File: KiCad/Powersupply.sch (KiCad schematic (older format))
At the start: 9 parts, among them J501 12V, U501 LM1086-5V, U502 LM1086-3.3V

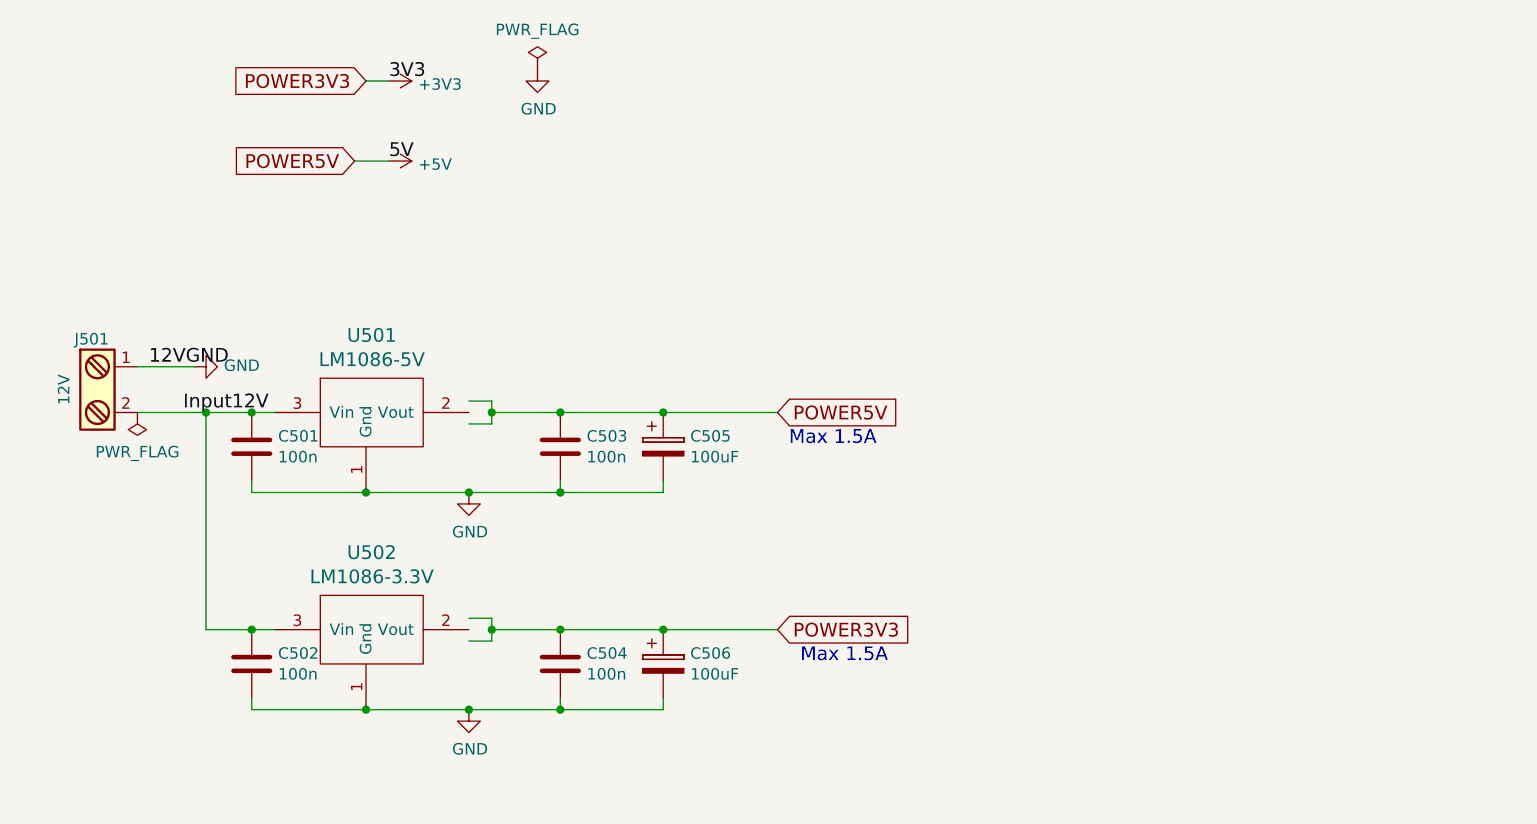
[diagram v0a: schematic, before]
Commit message: Before reworking analog inputs.
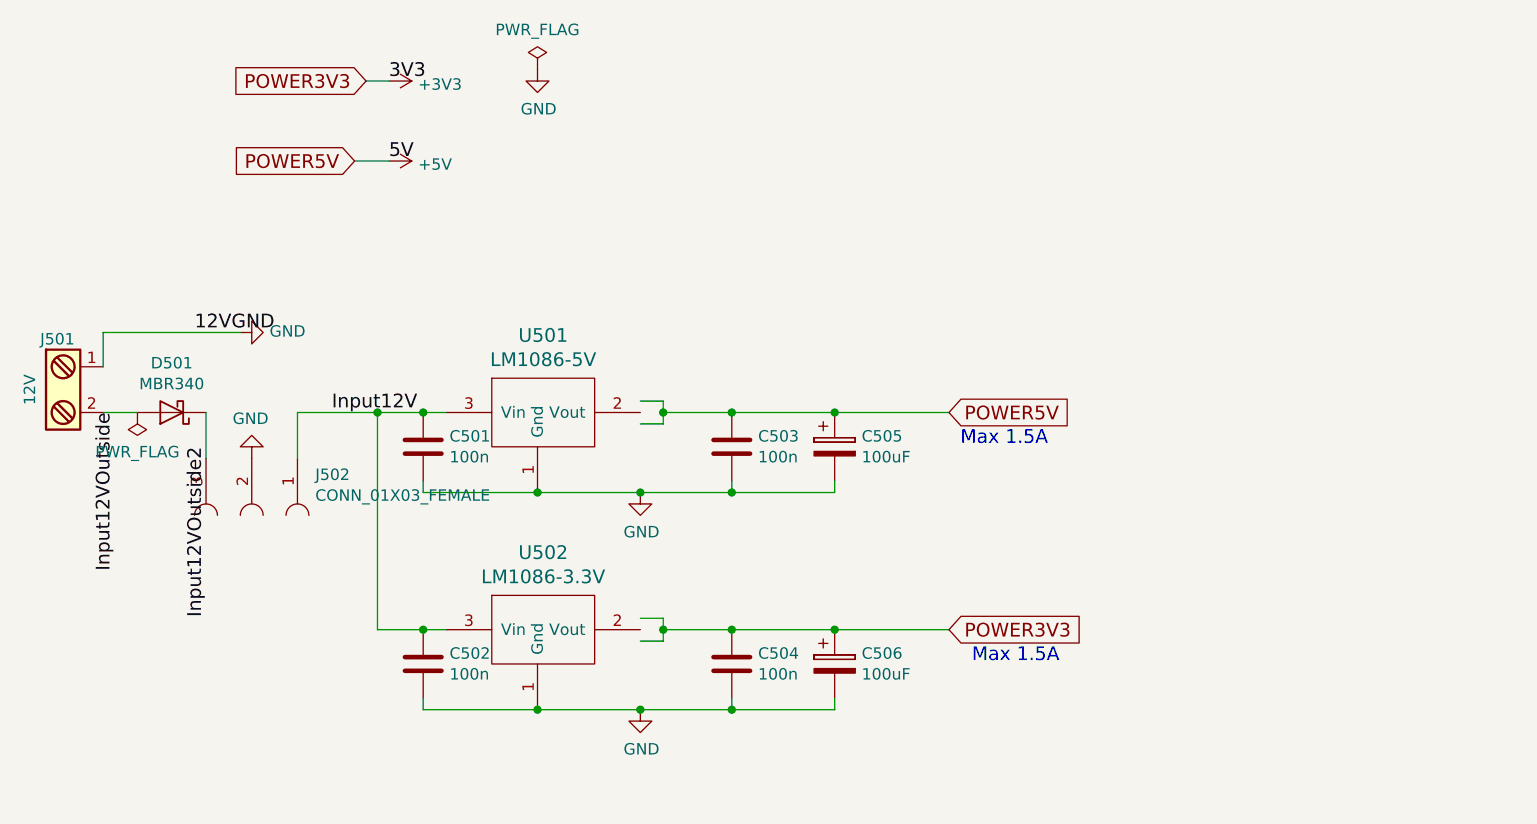
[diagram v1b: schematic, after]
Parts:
- added D501: MBR340, Diodes_SMD:D_SMB, symbol MBR340
- added J502: CONN_01X03_FEMALE, Pin_Headers:Pin_Header_Straight_1x03_Pitch2.54mm, symbol CONN_01X03_FEMALE
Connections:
- net labels added: Input12VOutside, Input12VOutside2
- wire segments 22 -> 26
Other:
- moved on the sheet: C501, C502, C503, C504, C505, C506, J501, U501, U502

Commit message: Save with sensor inputs using digital potentiometer
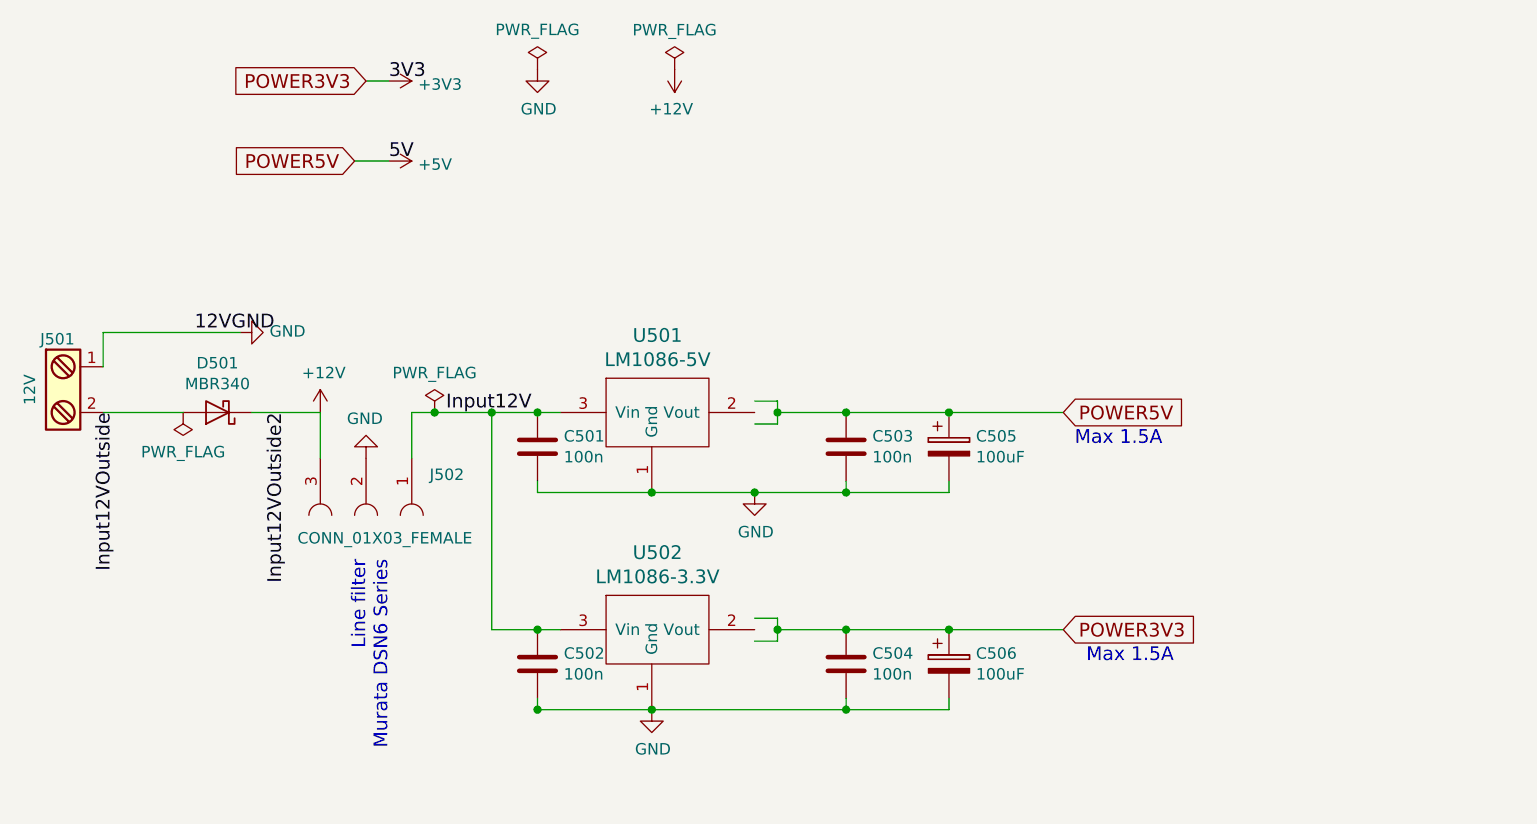
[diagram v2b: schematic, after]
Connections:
- net labels added: +12V
- wire segments 26 -> 27
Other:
- note added: "Line filter\nMurata DSN6 Series"
- moved on the sheet: C501, C502, C503, C504, C505, C506, D501, J502, U501, U502

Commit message: Inputs reworked. New terminals
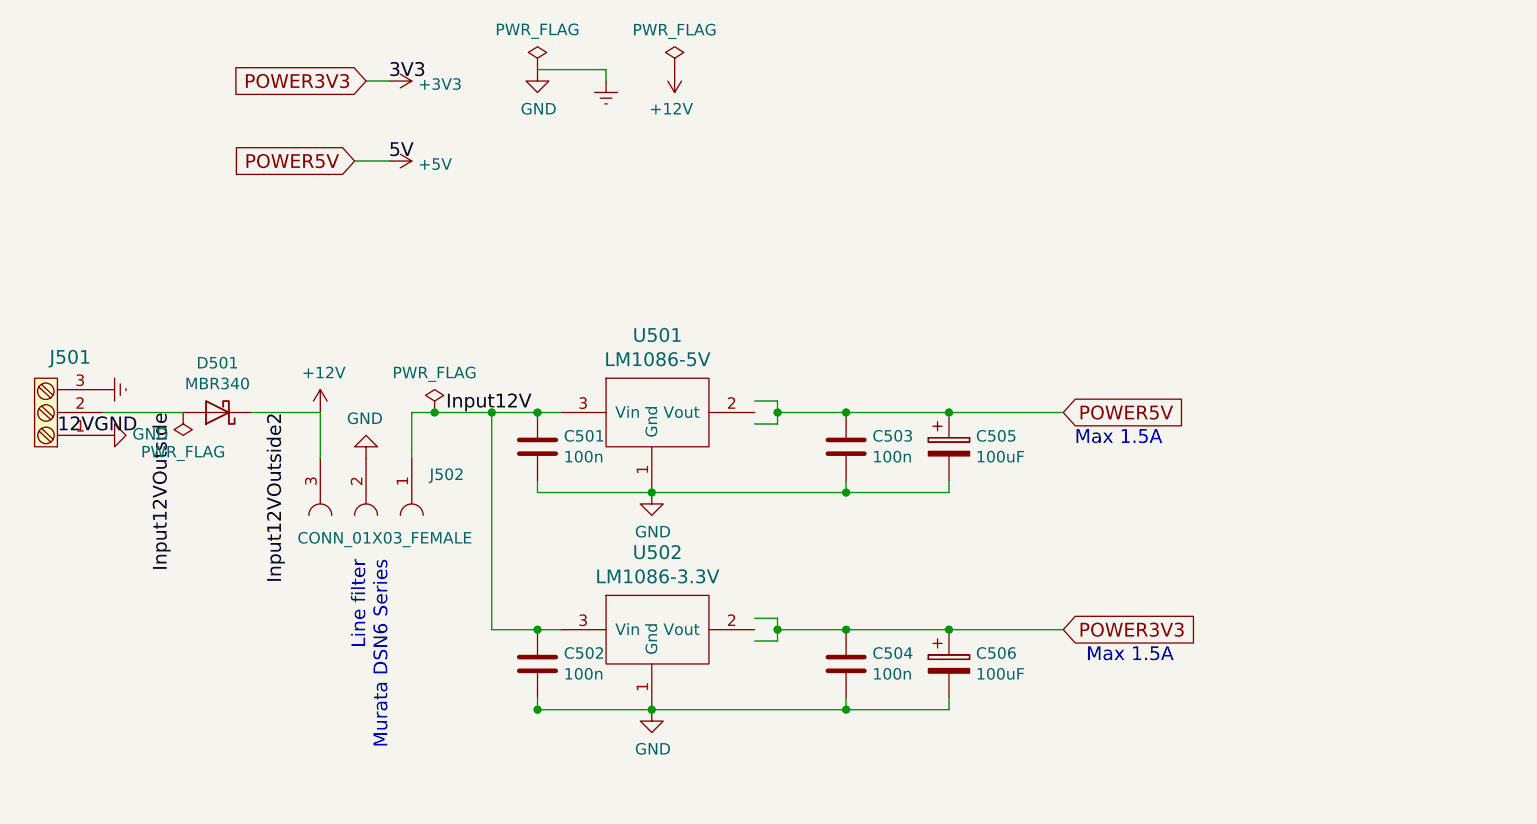
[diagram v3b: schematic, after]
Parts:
- removed J501: 12V, Connectors_Terminal_Blocks:TerminalBlock_Pheonix_MPT-2.54mm_2pol, symbol Screw_Terminal_1x02
- added J501: TE_Connectivity_282834-3, TE_Connectivity:TE_Connectivity_282834-3, symbol TE_Connectivity_282834-3
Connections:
- net labels added: Earth
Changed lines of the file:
@@
 LIBS:LM1086
 LIBS:X95840WV20IZ-2_7T1
-LIBS:804-112
+LIBS:TE_Connectivity
 LIBS:HAP-IO-Card-cache
 EELAYER 26 0
@@
 POWER3V3
 $Comp
-L +3V3 #PWR0118
+L +3V3 #PWR0104
 U 1 1 592AD7CB
 P 2200 1500
-F 0 "#PWR0118" H 2200 1350 50  0001 C CNN
+F 0 "#PWR0104" H 2200 1350 50  0001 C CNN
 F 1 "+3V3" V 2215 1628 50  0000 L CNN
 F 2 "" H 2200 1500 50  0001 C CNN
@@
 	2100 1500 2200 1500
 $Comp
-L PWR_FLAG #FLG0119
+L PWR_FLAG #FLG0105
 U 1 1 592B4E13
 P 2850 1450
-F 0 "#FLG0119" H 2850 1525 50  0001 C CNN
+F 0 "#FLG0105" H 2850 1525 50  0001 C CNN
 F 1 "PWR_FLAG" H 2850 1624 50  0000 C CNN
 F 2 "" H 2850 1450 50  0001 C CNN
@@
 $EndComp
 $Comp
-L GND #PWR0120
+L GND #PWR0106
 U 1 1 592B4E96
 P 2850 1450
-F 0 "#PWR0120" H 2850 1200 50  0001 C CNN
+F 0 "#PWR0106" H 2850 1200 50  0001 C CNN
 F 1 "GND" H 2855 1277 50  0000 C CNN
 F 2 "" H 2850 1450 50  0001 C CNN
@@
 $EndComp
 $Comp
-L GND #PWR0121
+L GND #PWR0107
 U 1 1 5924C039
 P 3350 4250
-F 0 "#PWR0121" H 3350 4000 50  0001 C CNN
+F 0 "#PWR0107" H 3350 4000 50  0001 C CNN
 F 1 "GND" H 3355 4077 50  0000 C CNN
 F 2 "" H 3350 4250 50  0001 C CNN
@@
 Connection ~ 4200 2950
 $Comp
-L GND #PWR0122
+L GND #PWR0108
 U 1 1 5924DE85
-P 1550 2600
-F 0 "#PWR0122" H 1550 2350 50  0001 C CNN
-F 1 "GND" V 1555 2472 50  0000 R CNN
-F 2 "" H 1550 2600 50  0001 C CNN
-F 3 "" H 1550 2600 50  0001 C CNN
-	1    1550 2600
+P 950 3050
+F 0 "#PWR0108" H 950 2800 50  0001 C CNN
+F 1 "GND" V 955 2922 50  0000 R CNN
+F 2 "" H 950 3050 50  0001 C CNN
+F 3 "" H 950 3050 50  0001 C CNN
+	1    950  3050
 	0    -1   -1   0
 $EndComp
 $Comp
-L PWR_FLAG #FLG0123
+L PWR_FLAG #FLG0109
 U 1 1 5924DE8B
 P 1300 2950
-F 0 "#FLG0123" H 1300 3025 50  0001 C CNN
+F 0 "#FLG0109" H 1300 3025 50  0001 C CNN
 F 1 "PWR_FLAG" H 1300 3123 50  0000 C CNN
 F 2 "" H 1300 2950 50  0001 C CNN
@@
 $EndComp
 Connection ~ 2850 2950
-$Comp
-L Screw_Terminal_1x02 J501
-U 1 1 5924DE7F
-P 750 2850
-F 0 "J501" H 750 3100 50  0000 C TNN
-F 1 "12V" V 600 2850 50  0000 C TNN
-F 2 "Connectors_Terminal_Blocks:TerminalBlock_Pheonix_MPT-2.54mm_2pol" H 750 2625 50  0001 C CNN
-F 3 "" H 725 2850 50  0001 C CNN
-	1    750  2850
-	1    0    0    -1
-$EndComp
 Wire Wire Line
 	2650 2950 2650 3900
@@
 	2050 1850 2200 1850
 $Comp
-L +5V #PWR0124
+L +5V #PWR0110
 U 1 1 5924EF19
 P 2200 1850
-F 0 "#PWR0124" H 2200 1700 50  0001 C CNN
+F 0 "#PWR0110" H 2200 1700 50  0001 C CNN
 F 1 "+5V" V 2215 1978 50  0000 L CNN
 F 2 "" H 2200 1850 50  0001 C CNN
@@
 $EndComp
 $Comp
-L GND #PWR0125
+L GND #PWR0111
 U 1 1 5924DE5E
-P 3800 3300
-F 0 "#PWR0125" H 3800 3050 50  0001 C CNN
-F 1 "GND" H 3805 3127 50  0000 C CNN
-F 2 "" H 3800 3300 50  0001 C CNN
-F 3 "" H 3800 3300 50  0001 C CNN
-	1    3800 3300
+P 3350 3300
+F 0 "#PWR0111" H 3350 3050 50  0001 C CNN
+F 1 "GND" H 3355 3127 50  0000 C CNN
+F 2 "" H 3350 3300 50  0001 C CNN
+F 3 "" H 3350 3300 50  0001 C CNN
+	1    3350 3300
 	1    0    0    -1
 $EndComp
@@
 Wire Wire Line
 	4200 3300 4200 3250
-Connection ~ 3800 3300
 Connection ~ 4200 3300
 Wire Wire Line
@@
 	1    0    0    -1
 $EndComp
-Wire Wire Line
-	950  2600 1550 2600
-Text Label 1350 2600 0    60   ~ 0
+Text Label 750  3050 0    60   ~ 0
 12VGND
 $Comp
@@
 	-1   0    0    1
 $EndComp
-Text Label 1000 2950 3    60   ~ 0
+Text Label 1250 2950 3    60   ~ 0
 Input12VOutside
 Wire Wire Line
@@
 $EndComp
 $Comp
-L GND #PWR0126
+L GND #PWR0112
 U 1 1 592909E6
 P 2100 3150
-F 0 "#PWR0126" H 2100 2900 50  0001 C CNN
+F 0 "#PWR0112" H 2100 2900 50  0001 C CNN
 F 1 "GND" H 2105 2977 50  0000 C CNN
 F 2 "" H 2100 3150 50  0001 C CNN
@@
 	-1   0    0    1
 $EndComp
-Wire Wire Line
-	950  2600 950  2750
 Text Label 1750 2950 3    60   ~ 0
 Input12VOutside2
@@
 	1900 2950 1900 3150
 $Comp
-L +12V #PWR0127
+L +12V #PWR0113
 U 1 1 592CA1C3
 P 1900 2950
-F 0 "#PWR0127" H 1900 2800 50  0001 C CNN
+F 0 "#PWR0113" H 1900 2800 50  0001 C CNN
 F 1 "+12V" H 1915 3123 50  0000 C CNN
 F 2 "" H 1900 2950 50  0001 C CNN
@@
 Connection ~ 4200 4250
 $Comp
-L PWR_FLAG #FLG0128
+L PWR_FLAG #FLG0114
 U 1 1 592E87DD
 P 3450 1450
-F 0 "#FLG0128" H 3450 1525 50  0001 C CNN
+F 0 "#FLG0114" H 3450 1525 50  0001 C CNN
 F 1 "PWR_FLAG" H 3450 1623 50  0000 C CNN
 F 2 "" H 3450 1450 50  0001 C CNN
@@
 $EndComp
 $Comp
-L +12V #PWR0129
+L +12V #PWR0115
 U 1 1 592E8840
 P 3450 1450
-F 0 "#PWR0129" H 3450 1300 50  0001 C CNN
+F 0 "#PWR0115" H 3450 1300 50  0001 C CNN
 F 1 "+12V" H 3465 1623 50  0000 C CNN
 F 2 "" H 3450 1450 50  0001 C CNN
@@
 $EndComp
 $Comp
-L PWR_FLAG #FLG0130
+L PWR_FLAG #FLG0116
 U 1 1 592EF7D9
 P 2400 2950
-F 0 "#FLG0130" H 2400 3025 50  0001 C CNN
+F 0 "#FLG0116" H 2400 3025 50  0001 C CNN
 F 1 "PWR_FLAG" H 2400 3123 50  0000 C CNN
 F 2 "" H 2400 2950 50  0001 C CNN
@@
 	2300 2950 2300 3150
 Connection ~ 2400 2950
+$Comp
+L Earth #PWR0117
+U 1 1 5933481E
+P 950 2850
+F 0 "#PWR0117" H 950 2600 50  0001 C CNN
+F 1 "Earth" H 950 2700 50  0001 C CNN
+F 2 "" H 950 2850 50  0001 C CNN
+F 3 "" H 950 2850 50  0001 C CNN
+	1    950  2850
+	0    -1   -1   0
+$EndComp
+$Comp
+L TE_Connectivity_282834-3 J501
+U 1 1 5934471B
+P 950 2950
+F 0 "J501" H 1094 2709 60  0000 C CNN
+F 1 "TE_Connectivity_282834-3" H 1223 2746 60  0001 C CNN
+F 2 "TE_Connectivity:TE_Connectivity_282834-3" H 950 2950 60  0001 C CNN
+F 3 "" H 950 2950 60  0001 C CNN
+	1    950  2950
+	-1   0    0    1
+$EndComp
+$Comp
+L Earth #PWR0118
+U 1 1 59344C28
+P 3150 1500
+F 0 "#PWR0118" H 3150 1250 50  0001 C CNN
+F 1 "Earth" H 3150 1350 50  0001 C CNN
+F 2 "" H 3150 1500 50  0001 C CNN
+F 3 "" H 3150 1500 50  0001 C CNN
+	1    3150 1500
+	1    0    0    -1
+$EndComp
+Wire Wire Line
+	3150 1500 3150 1450
+Wire Wire Line
+	3150 1450 2850 1450
 $EndSCHEMATC
